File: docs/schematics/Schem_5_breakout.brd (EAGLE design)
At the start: 160 x 100 mm, 36 parts, among them CON1 TEC 5103308-01, J3 POWER_JACK, T1 2N2222, T2 2N2222, U1 AT89S52, U2 DS1621S, U3 7805TV, Y1 12MHz

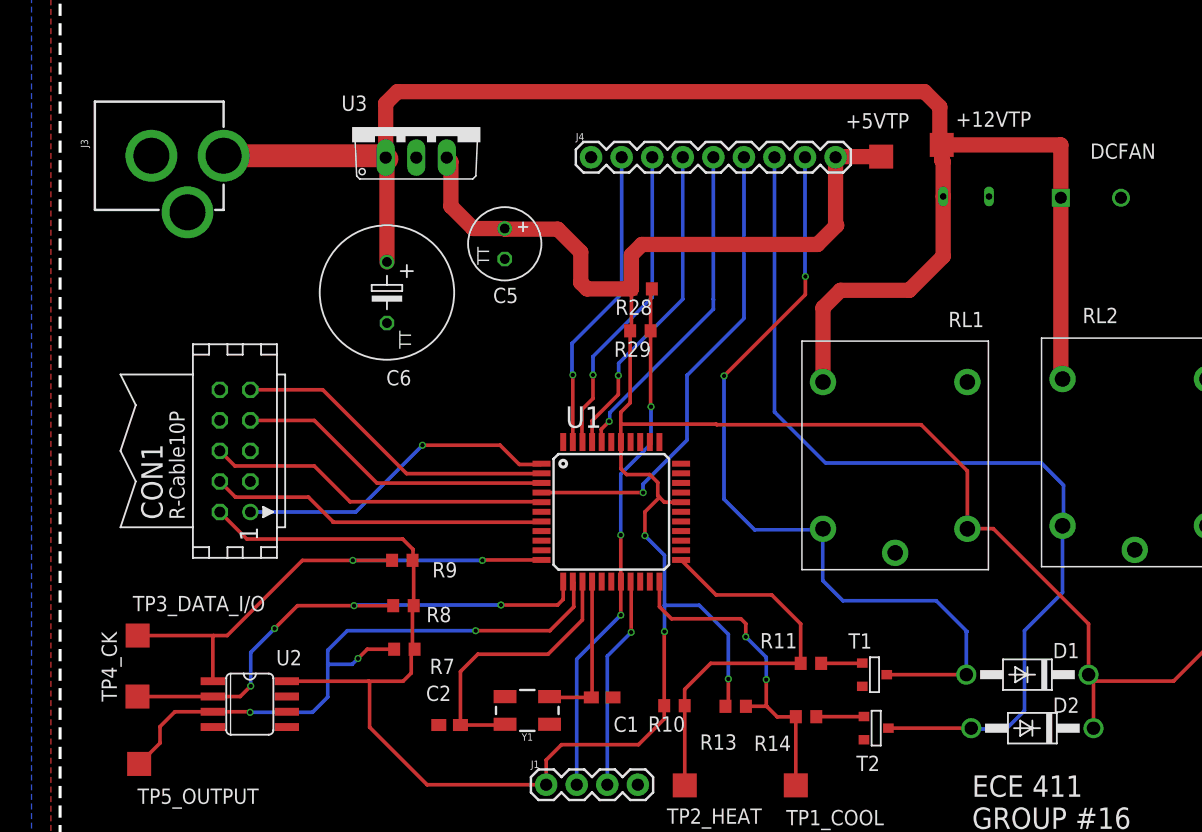
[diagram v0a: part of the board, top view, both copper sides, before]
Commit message: Edited component name and value locations
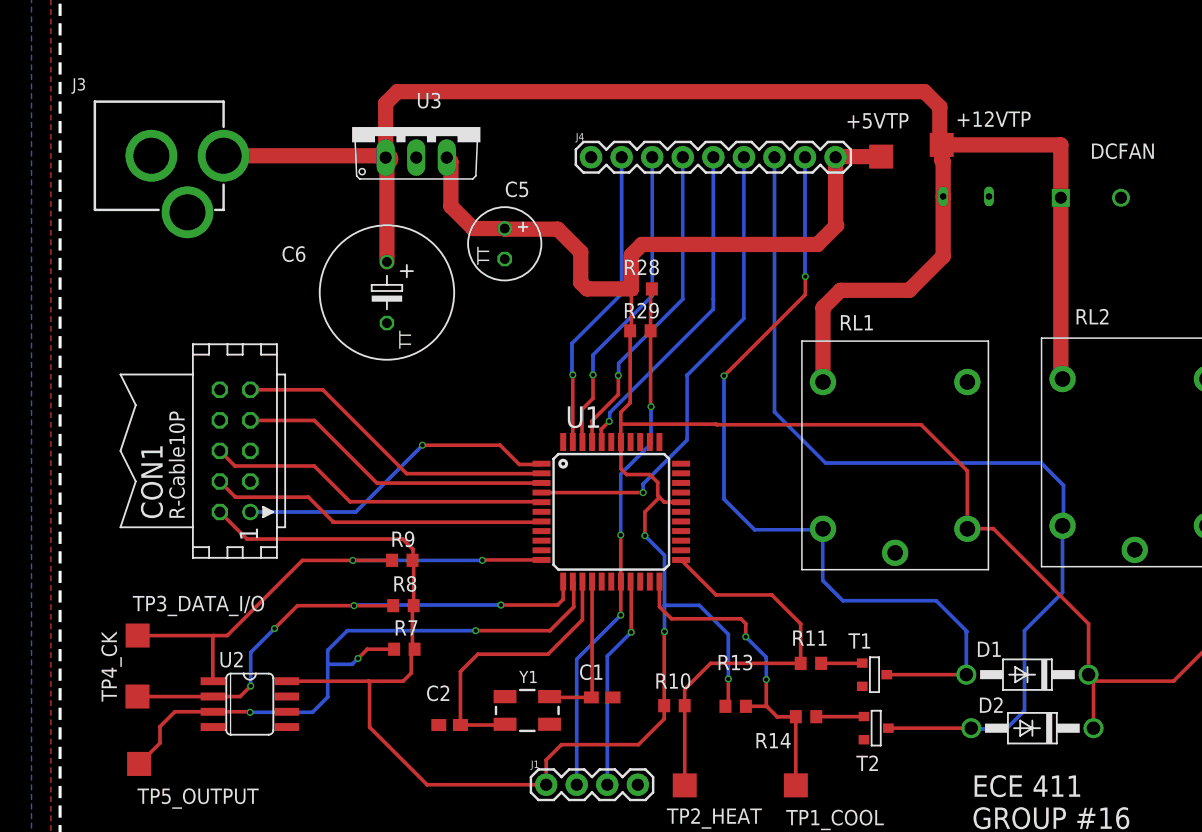
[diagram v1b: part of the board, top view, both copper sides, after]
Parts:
- renumbered U$18 to LIGHTBULB
